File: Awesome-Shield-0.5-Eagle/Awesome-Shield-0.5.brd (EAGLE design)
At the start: 100 x 80 mm, 24 parts, among them J1 ARDUINO_R3_SHIELDUNO_R3_SHIEL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, SW1 SPST_TACT-EVQQ2

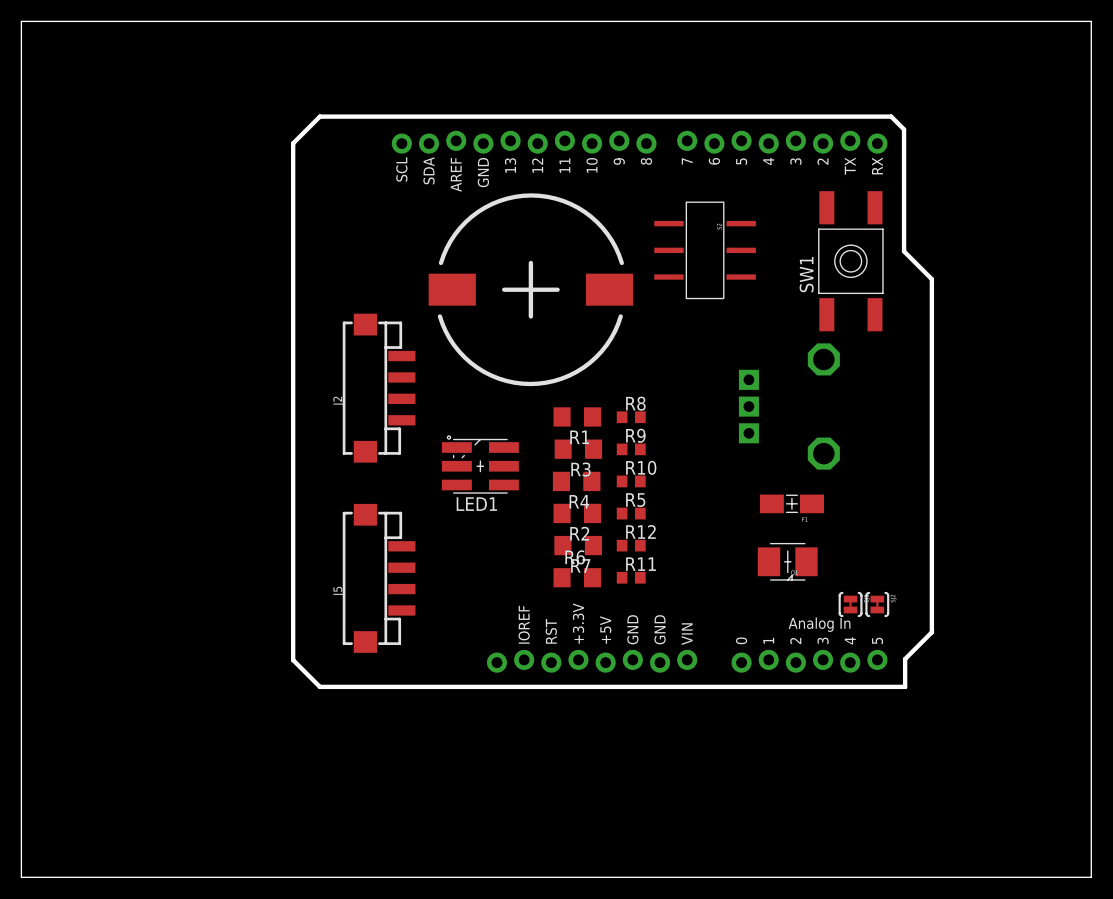
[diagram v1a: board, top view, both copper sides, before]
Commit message: completed routing traces for CPvar2
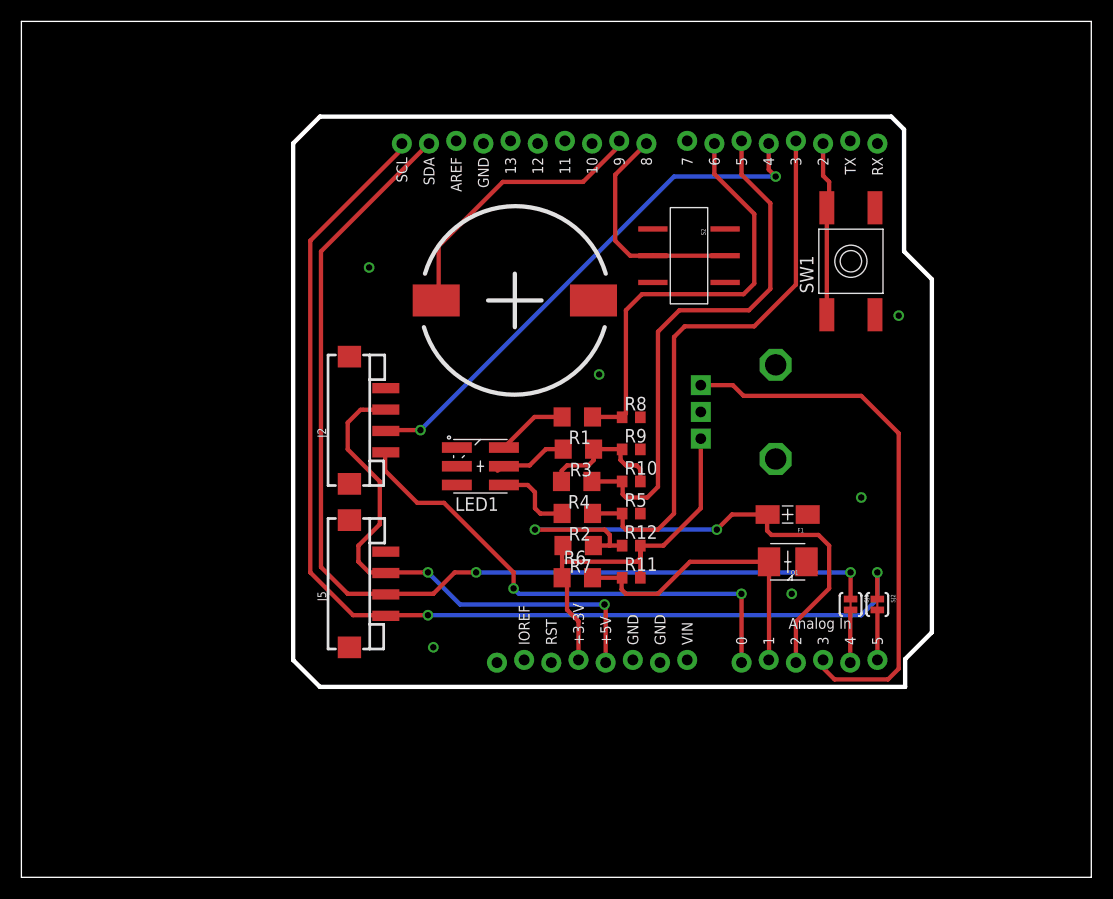
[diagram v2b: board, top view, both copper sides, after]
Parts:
- moved RV1 4.53 mm to (70.5, 43.5)
- moved J2 3.35 mm to (34.1, 42.7)
- moved SG1 1.80 mm to (46.1, 53.9)
- moved J5 1.58 mm to (34.1, 27.4)
- moved S2 1.58 mm to (62.4, 58.1)
- moved F1 1.08 mm to (71.6, 33.9)
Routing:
- net SCL: track 0.00 -> 103.9 mm, vias 0 -> 2
- net SDA: track 0.00 -> 97.7 mm, vias 0 -> 2
- net A2: track 0.00 -> 53.3 mm, vias 0 -> 2
- net D3: track 0.00 -> 52.9 mm
- net A3: track 0.00 -> 51.0 mm
- net D4: track 0.00 -> 49.6 mm, vias 0 -> 2
- net D5: track 0.00 -> 49.5 mm
- net +5V: track 0.00 -> 49.3 mm, vias 0 -> 2
- net A0: track 0.00 -> 47.1 mm, vias 0 -> 2
- net D6: track 0.00 -> 40.3 mm
- net +3V3: track 0.00 -> 36.6 mm
- net A1: track 0.00 -> 28.3 mm
- net D9: track 0.00 -> 26.4 mm
- net D8: track 0.00 -> 21.1 mm
- net D2: track 0.00 -> 16.3 mm
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
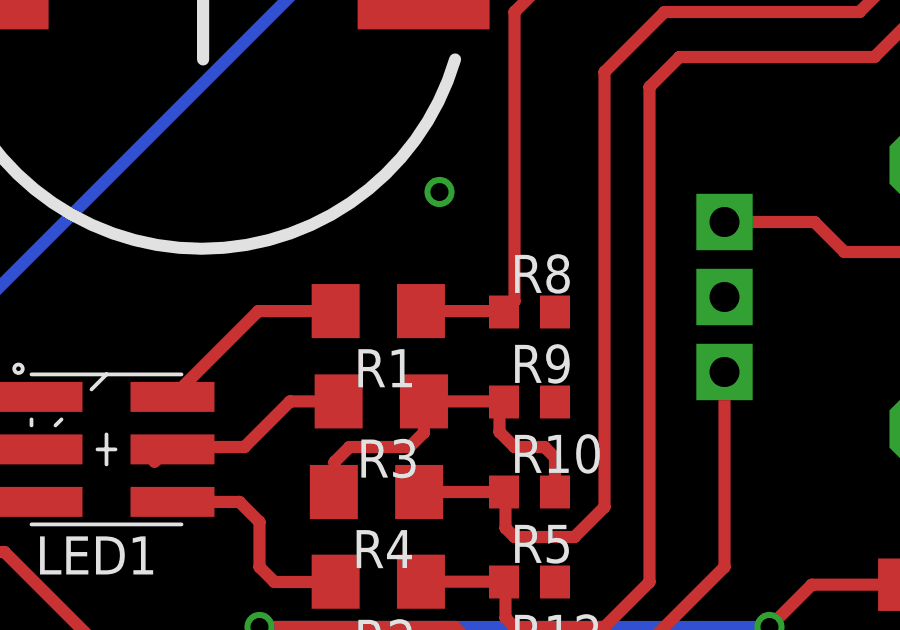
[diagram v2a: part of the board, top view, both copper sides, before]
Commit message: added missing connections between resitors
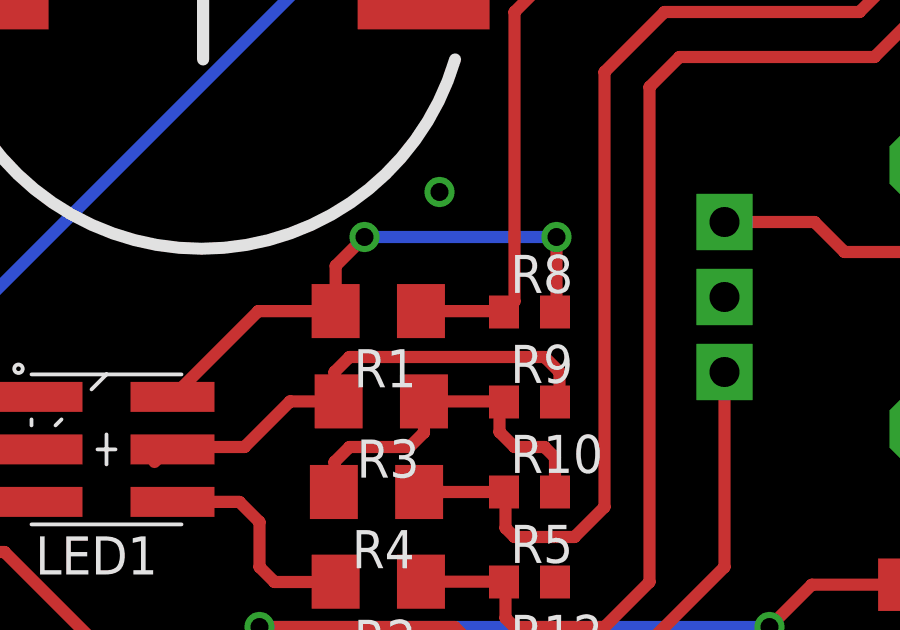
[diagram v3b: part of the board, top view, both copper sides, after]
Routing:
- net N$8: track 6.62 -> 18.4 mm, vias 0 -> 2
- net N$3: track 6.97 -> 17.1 mm
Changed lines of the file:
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@@
 <wire x1="47.5" y1="38.5" x2="45" y2="38.5" width="0.4064" layer="1"/>
 <wire x1="45" y1="38.5" x2="44.5" y2="38" width="0.4064" layer="1"/>
-<wire x1="50.638" y1="40.02" x2="57.85" y2="40" width="0" layer="19" extent="1-1"/>
-<wire x1="45.1" y1="38.42" x2="45" y2="38.5" width="0" layer="19" extent="1-1"/>
+<wire x1="57.85" y1="40" x2="58" y2="40" width="0.4064" layer="1"/>
+<wire x1="58" y1="40" x2="58" y2="41" width="0.4064" layer="1"/>
+<wire x1="58" y1="41" x2="57.5" y2="41.5" width="0.4064" layer="1"/>
+<wire x1="57.5" y1="41.5" x2="51" y2="41.5" width="0.4064" layer="1"/>
+<wire x1="51" y1="41.5" x2="50.5" y2="41" width="0.4064" layer="1"/>
+<wire x1="50.5" y1="41" x2="50.5" y2="40.158" width="0.4064" layer="1"/>
+<wire x1="50.5" y1="40.158" x2="50.638" y2="40.02" width="0.4064" layer="1"/>
+<wire x1="45" y1="38.5" x2="45.1" y2="38.42" width="0" layer="19" extent="1-1"/>
 </signal>
 <signal name="D2">
@@
 <wire x1="50.538" y1="43.03" x2="47.96" y2="43.03" width="0.4064" layer="1"/>
 <wire x1="47.96" y1="43.03" x2="45.1" y2="40.17" width="0.4064" layer="1"/>
-<wire x1="50.538" y1="43.03" x2="57.85" y2="43" width="0" layer="19" extent="1-1"/>
+<wire x1="50.538" y1="43.03" x2="50.538" y2="44.538" width="0.4064" layer="1"/>
+<wire x1="50.538" y1="44.538" x2="51.5" y2="45.5" width="0.4064" layer="1"/>
+<via x="51.5" y="45.5" extent="1-16" drill="0.6" shape="square"/>
+<wire x1="51.5" y1="45.5" x2="57.9" y2="45.5" width="0.4064" layer="16"/>
+<via x="57.9" y="45.5" extent="1-16" drill="0.6" shape="square"/>
+<wire x1="57.9" y1="45.5" x2="57.9" y2="43.05" width="0.4064" layer="1"/>
+<wire x1="57.9" y1="43.05" x2="57.85" y2="43" width="0.4064" layer="1"/>
 </signal>
 <signal name="D3">

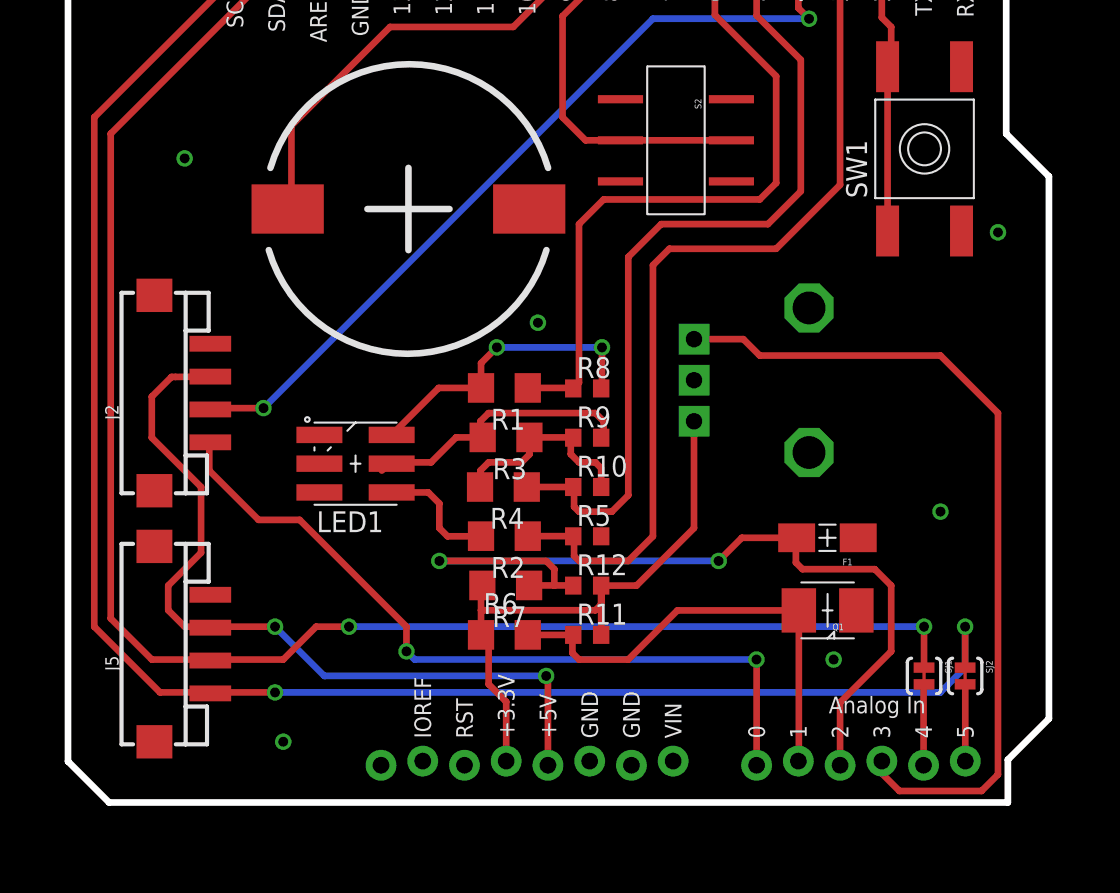
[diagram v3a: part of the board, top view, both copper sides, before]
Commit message: fixed silkscreen to comply with DRC
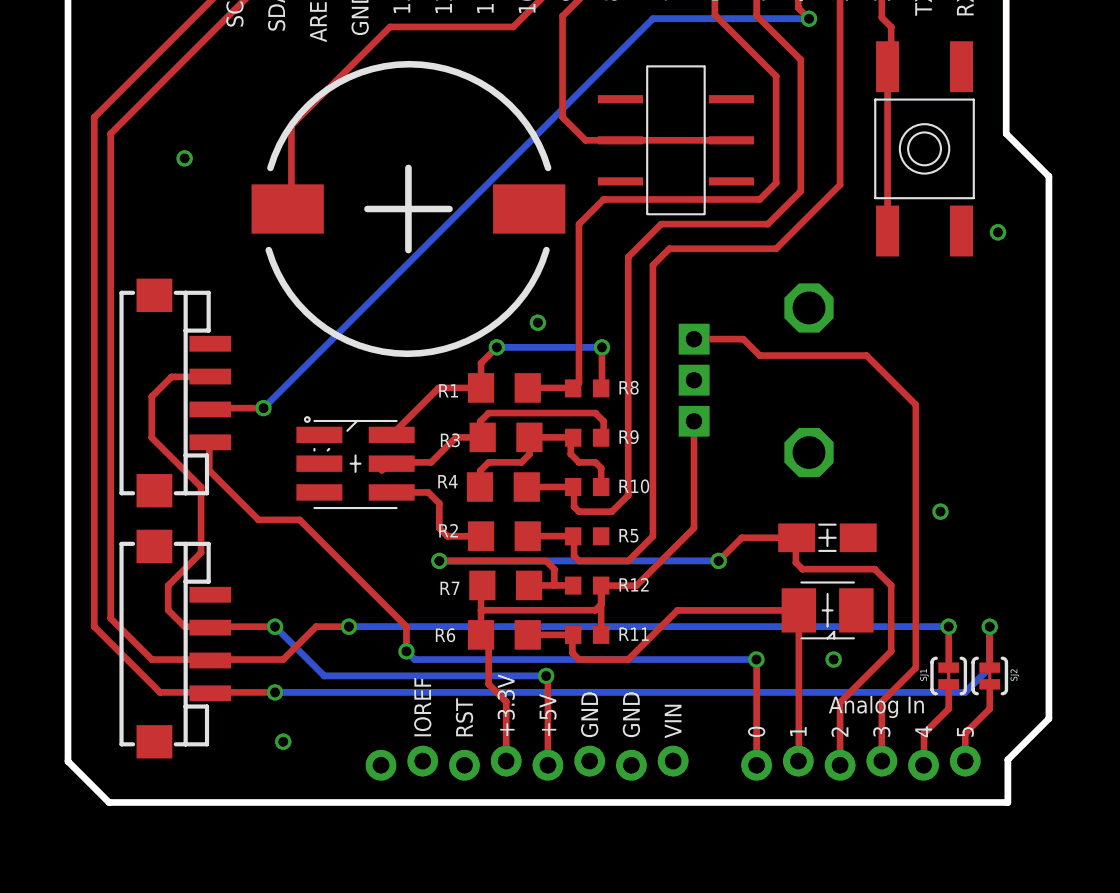
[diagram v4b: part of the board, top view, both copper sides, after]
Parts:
- moved SJ1 1.50 mm to (79.0, 25.5)
- moved SJ2 1.50 mm to (81.5, 25.5)
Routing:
- net A3: track 51.0 -> 37.7 mm
- net SDA: track 97.7 -> 99.2 mm
- net SCL: track 103.9 -> 105.4 mm
- net A4: track 4.94 -> 5.60 mm
- net A5: track 4.68 -> 5.31 mm

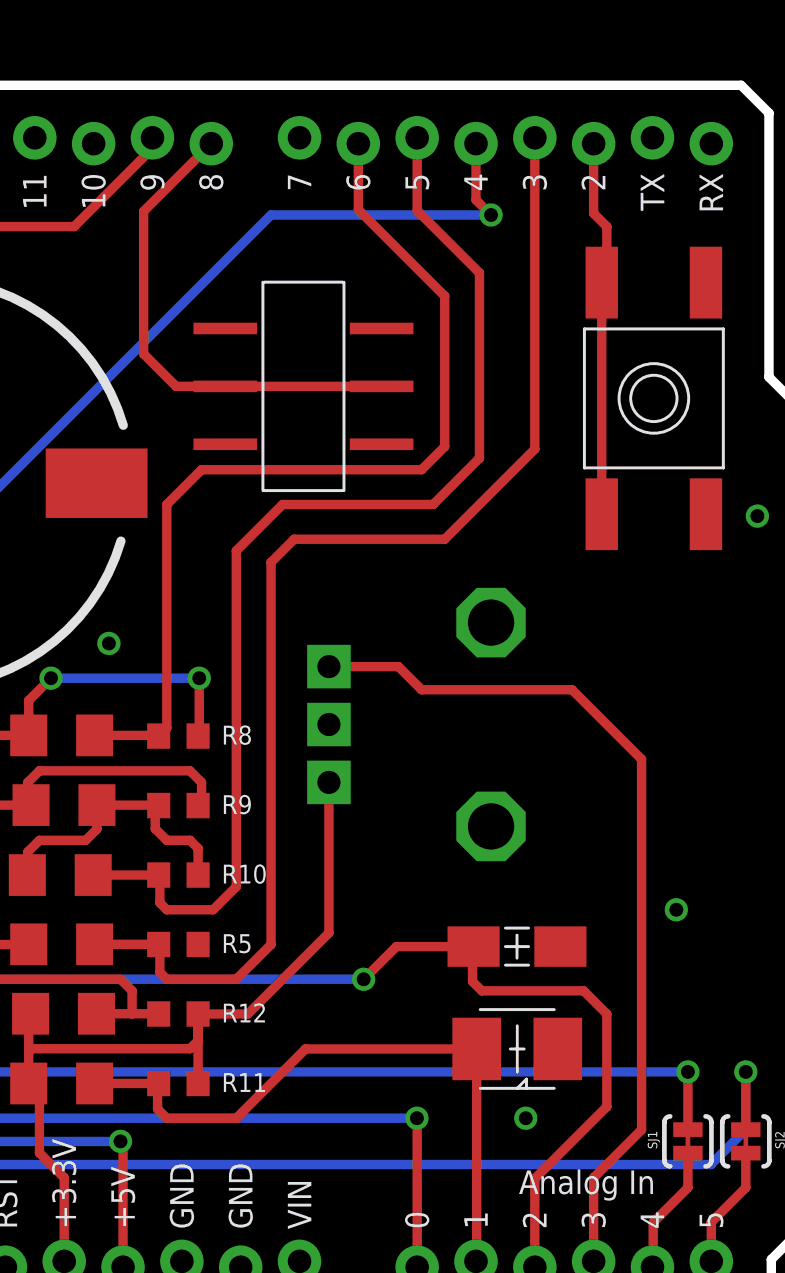
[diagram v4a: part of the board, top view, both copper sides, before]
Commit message: nudged traces for GND pour
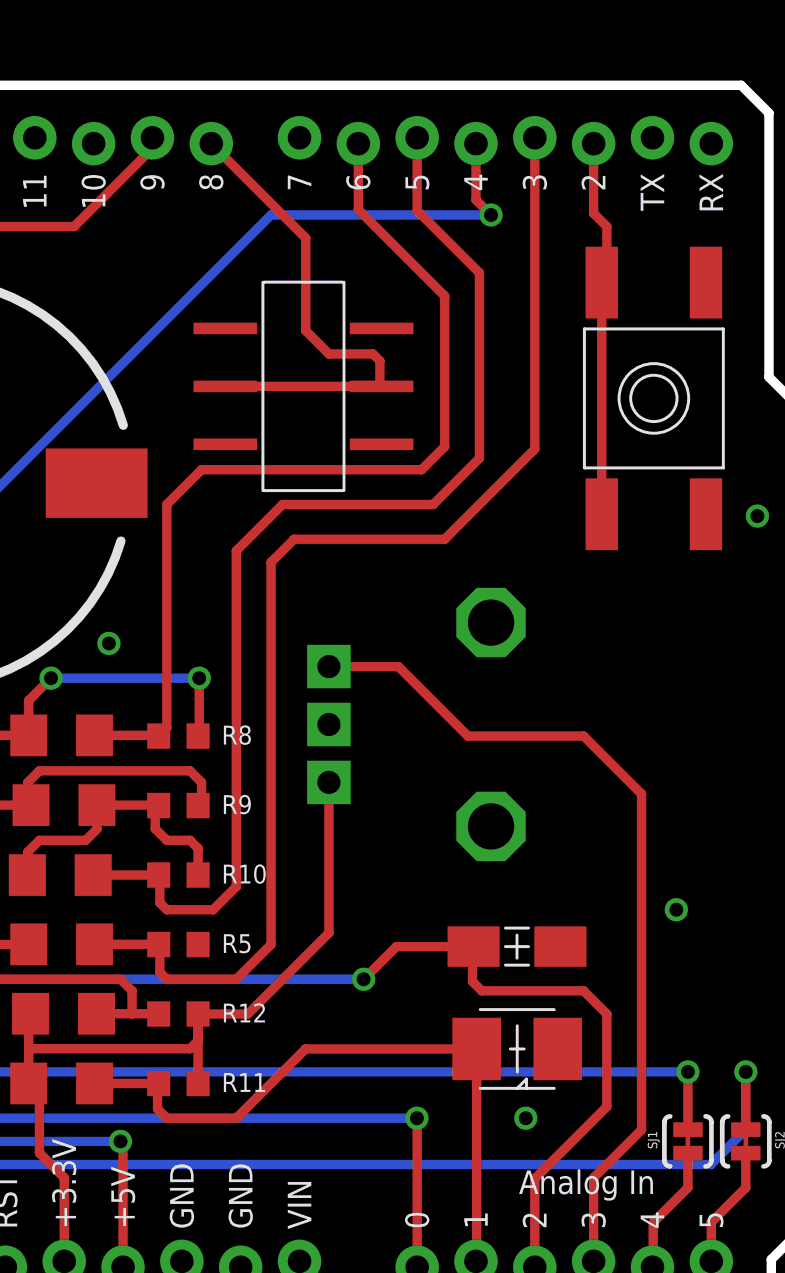
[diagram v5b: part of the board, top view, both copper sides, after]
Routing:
- net A3: track 37.7 -> 36.8 mm
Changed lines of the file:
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@@
 <contactref element="J1" pad="D8"/>
 <wire x1="65.775" y1="58.1" x2="59.025" y2="58.1" width="0.4064" layer="1"/>
-<wire x1="59.025" y1="58.1" x2="56.9" y2="58.1" width="0.4064" layer="1"/>
-<wire x1="56.9" y1="58.1" x2="55.5" y2="59.5" width="0.4064" layer="1"/>
-<wire x1="55.5" y1="59.5" x2="55.5" y2="65.66" width="0.4064" layer="1"/>
-<wire x1="55.5" y1="65.66" x2="58.42" y2="68.58" width="0.4064" layer="1"/>
+<wire x1="58.42" y1="68.58" x2="62.5" y2="64.5" width="0.4064" layer="1"/>
+<wire x1="62.5" y1="64.5" x2="62.5" y2="60.5" width="0.4064" layer="1"/>
+<wire x1="62.5" y1="60.5" x2="63.5" y2="59.5" width="0.4064" layer="1"/>
+<wire x1="63.5" y1="59.5" x2="65.4" y2="59.5" width="0.4064" layer="1"/>
+<wire x1="65.4" y1="59.5" x2="65.7" y2="59.2" width="0.4064" layer="1"/>
+<wire x1="65.7" y1="59.2" x2="65.7" y2="58.175" width="0.4064" layer="1"/>
+<wire x1="65.7" y1="58.175" x2="65.775" y2="58.1" width="0.4064" layer="1"/>
 </signal>
 <signal name="D9">
@@
 <contactref element="J1" pad="A3"/>
 <contactref element="RV1" pad="P$1"/>
-<wire x1="74" y1="45" x2="67.5" y2="45" width="0.4064" layer="1"/>
-<wire x1="67.5" y1="45" x2="66.5" y2="46" width="0.4064" layer="1"/>
 <wire x1="66.5" y1="46" x2="63.5" y2="46" width="0.4064" layer="1"/>
 <wire x1="74.93" y1="20.32" x2="74.93" y2="23.93" width="0.4064" layer="1"/>
 <wire x1="74.93" y1="23.93" x2="77" y2="26" width="0.4064" layer="1"/>
-<wire x1="77" y1="26" x2="77" y2="42" width="0.4064" layer="1"/>
-<wire x1="77" y1="42" x2="74" y2="45" width="0.4064" layer="1"/>
+<wire x1="77" y1="26" x2="77" y2="40.5" width="0.4064" layer="1"/>
+<wire x1="77" y1="40.5" x2="74.5" y2="43" width="0.4064" layer="1"/>
+<wire x1="74.5" y1="43" x2="69.5" y2="43" width="0.4064" layer="1"/>
+<wire x1="69.5" y1="43" x2="66.5" y2="46" width="0.4064" layer="1"/>
 </signal>
 </signals>
